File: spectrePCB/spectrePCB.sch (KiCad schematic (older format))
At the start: 21 parts

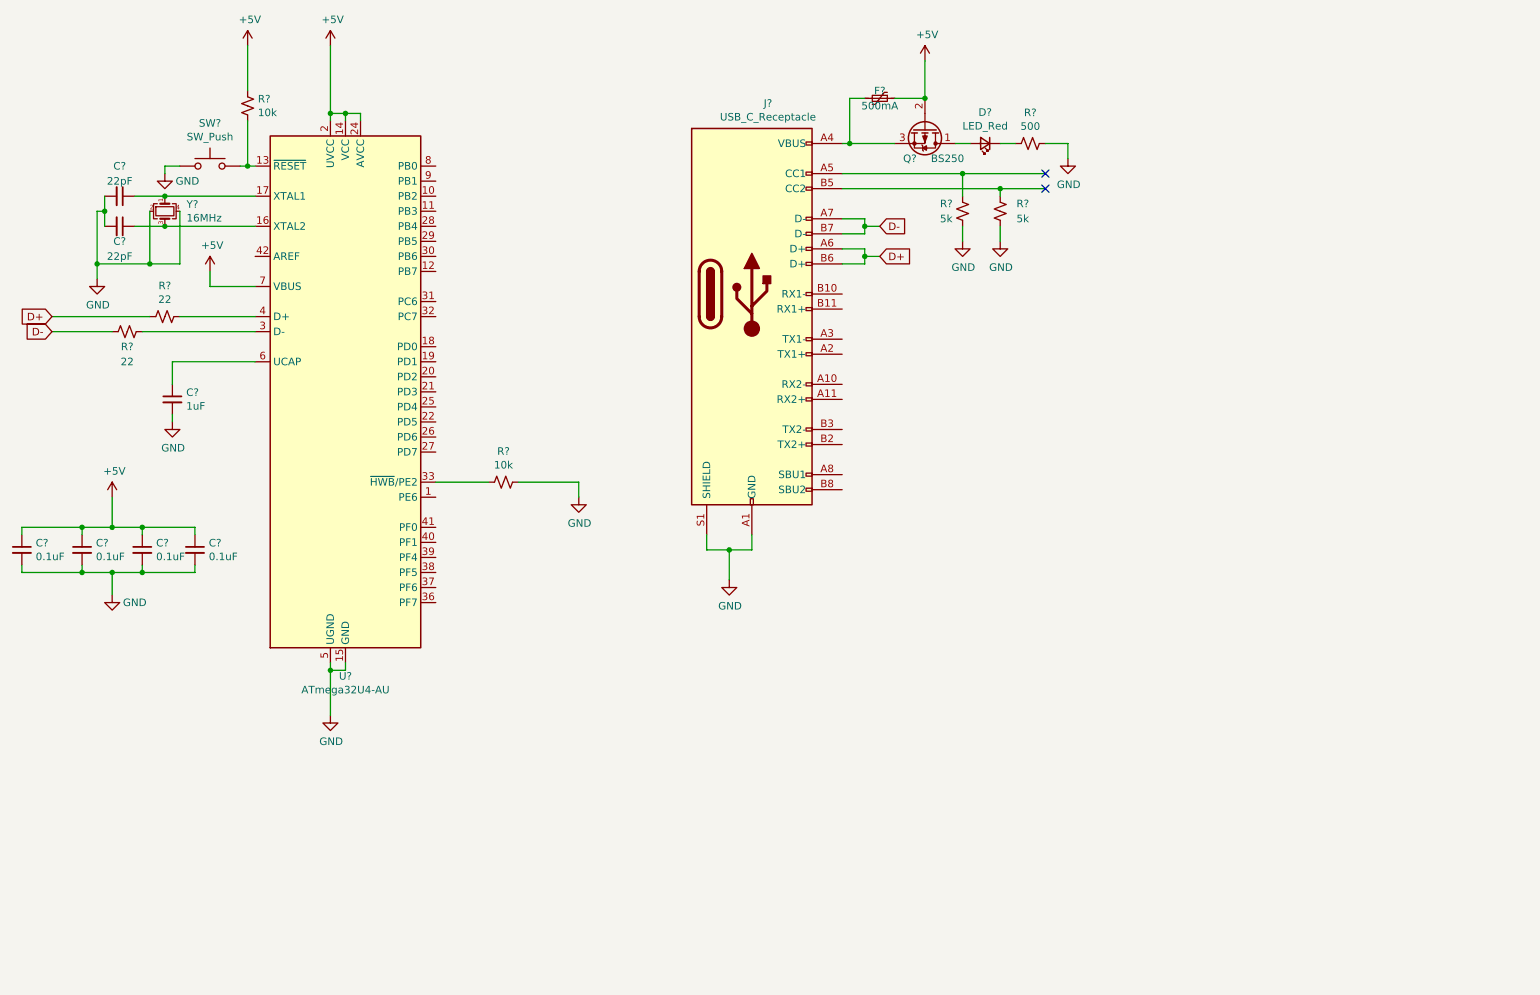
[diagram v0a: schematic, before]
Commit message: added switch and led matricies and pinouts to atmega
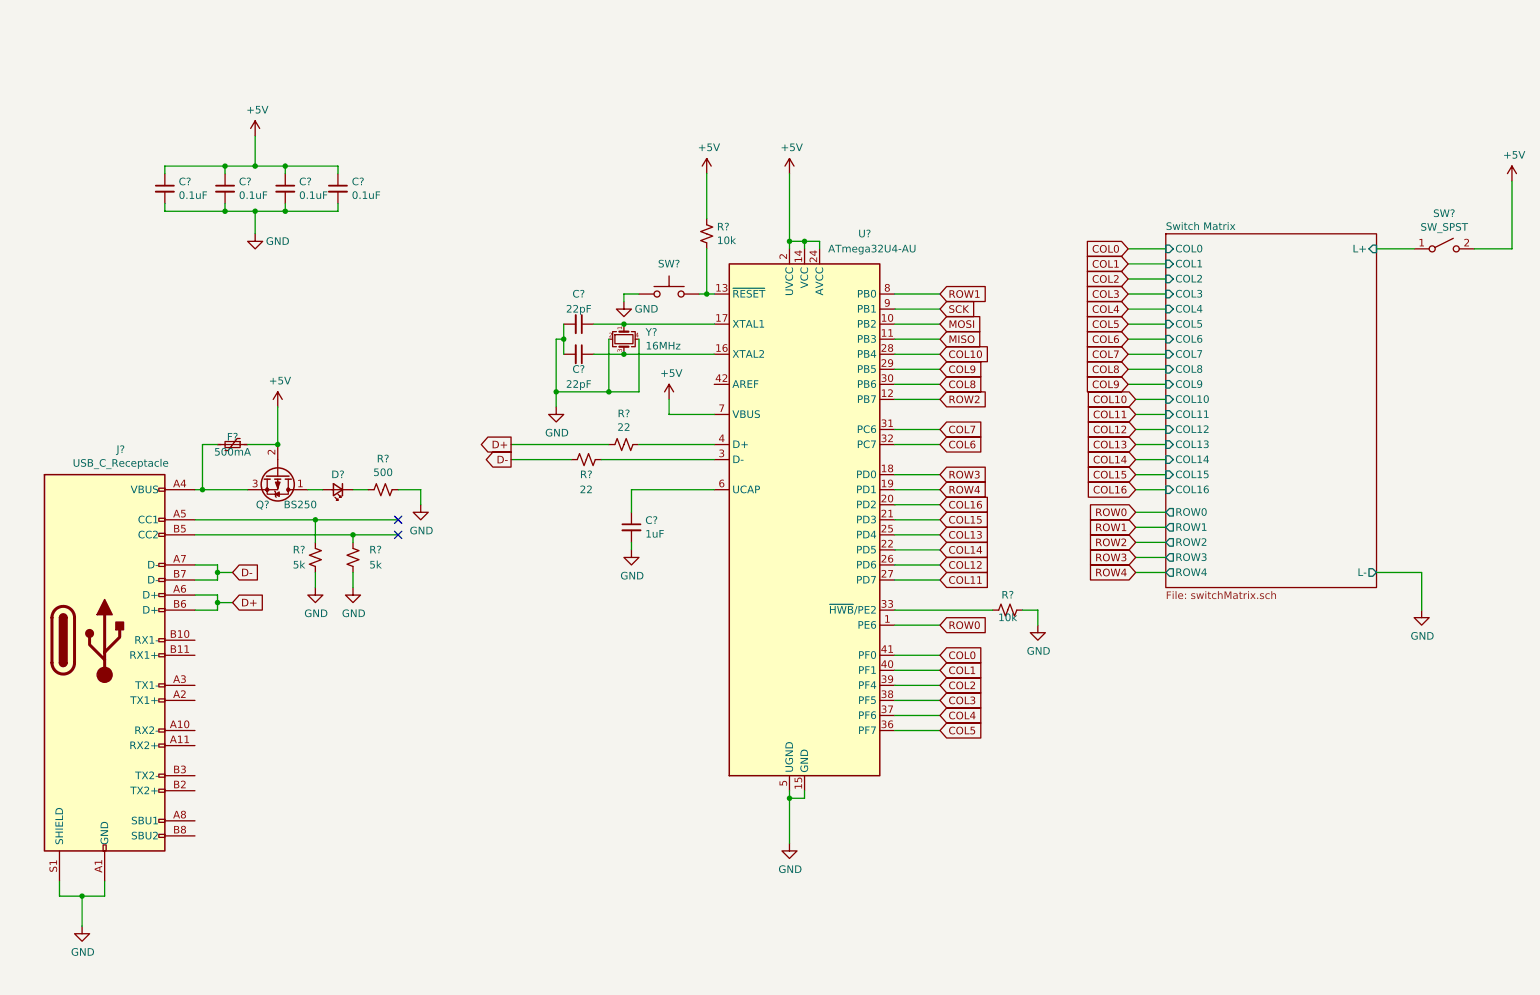
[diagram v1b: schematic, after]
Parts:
- added SW?: SW_SPST, symbol Switch:SW_SPST
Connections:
- net +5V: now also SW?.2 (B)
- net ROW0: now reaches U?.1 (PE6)
- net MOSI: now reaches U?.10 (PB2)
- net MISO: now reaches U?.11 (PB3)
- net ROW2: now reaches U?.12 (PB7)
- net ROW3: now reaches U?.18 (PD0)
- net ROW4: now reaches U?.19 (PD1)
- net COL16: now reaches U?.20 (PD2)
- net COL15: now reaches U?.21 (PD3)
- net COL14: now reaches U?.22 (PD5)
- net COL13: now reaches U?.25 (PD4)
- net COL12: now reaches U?.26 (PD6)
- net COL11: now reaches U?.27 (PD7)
- net COL10: now reaches U?.28 (PB4)
- net COL9: now reaches U?.29 (PB5)
- net COL8: now reaches U?.30 (PB6)
- net COL7: now reaches U?.31 (PC6)
- net COL6: now reaches U?.32 (PC7)
- net COL5: now reaches U?.36 (PF7)
- net COL4: now reaches U?.37 (PF6)
- net COL3: now reaches U?.38 (PF5)
- net COL2: now reaches U?.39 (PF4)
- net COL1: now reaches U?.40 (PF1)
- net COL0: now reaches U?.41 (PF0)
- net ROW1: now reaches U?.8 (PB0)
- net SCK: now reaches U?.9 (PB1)
- new net Switch Matrix/L+: SW?.1 (A)
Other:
- moved on the sheet: C?, D?, F?, J?, Q?, R?, SW?, U?, Y?

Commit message: finished capslock key and pin mapping. Rev1 done
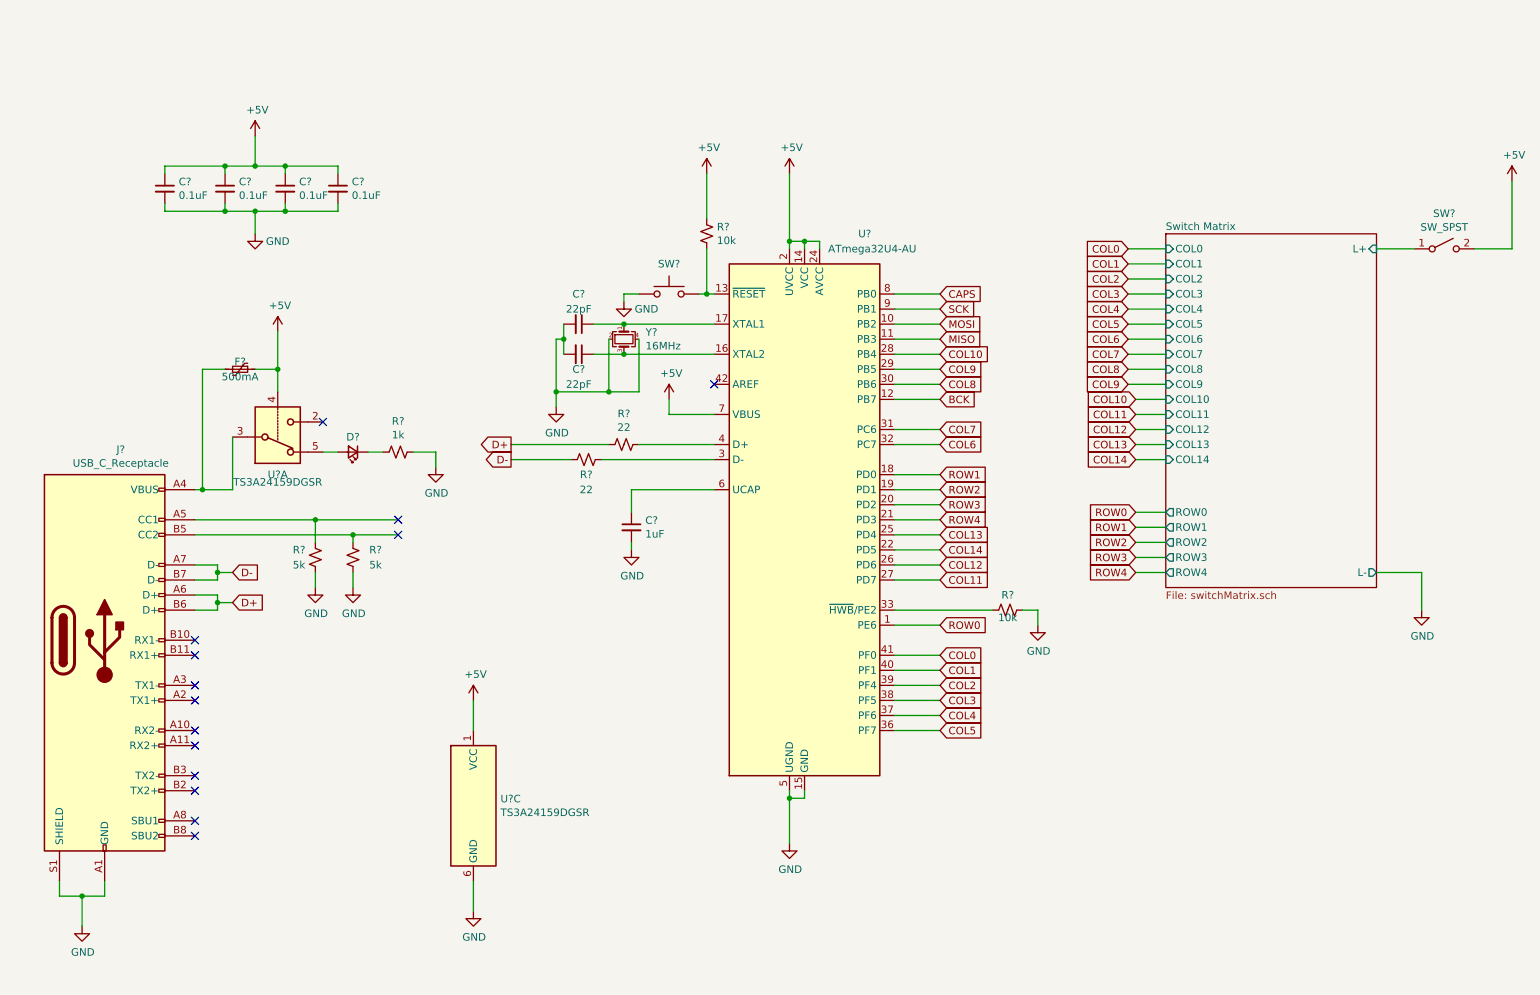
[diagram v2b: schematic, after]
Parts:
- removed Q?: BS250, Package_TO_SOT_THT:TO-92_Inline, symbol Transistor_FET:BS250
- added U? (x2): TS3A24159DGSR, Package_SO:TSSOP-10_3x3mm_P0.5mm, symbol Analog_Switch:TS3A24159DGSR
- R?: value 500 -> 1k
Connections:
- net COL15 is gone; now on net ROW4: U?.21 (PD3)
- net COL16 is gone; now on net ROW3: U?.20 (PD2)
- net +5V: now also U?.1 (VCC), U?.4
- net GND: now also U?.6 (GND)
- net ROW1: now also U?.18 (PD0); no longer U?.8 (PB0)
- net ROW2: now also U?.19 (PD1); no longer U?.12 (PB7)
- net ROW3: no longer U?.18 (PD0)
- net ROW4: no longer U?.19 (PD1)
- net at F?.2, J?.A4 (VBUS), J?.A9 (VBUS)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: now also U?.3
- net at D?.2 (A): now also U?.5
- new net BCK: U?.12 (PB7)
- new net CAPS: U?.8 (PB0)
- no-connect marks 2 -> 14
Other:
- moved on the sheet: D?, F?, R?
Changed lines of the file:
@@
 F20 "COL13" I L 8300 3500 50
 F21 "COL14" I L 8300 3600 50
-F22 "COL15" I L 8300 3700 50
-F23 "COL16" I L 8300 3800 50
-F24 "L+" I R 9700 2200 50
-F25 "L-" O R 9700 4350 50
+F22 "L+" I R 9700 2200 50
+F23 "L-" O R 9700 4350 50
 $EndSheet
-Connection ~ 2400 3500
-Wire Wire Line
-	2400 3500 2400 3250
-Wire Wire Line
-	3350 3800 3350 3900
-Wire Wire Line
-	3200 3800 3350 3800
-$Comp
-L power:GND #PWR?
-U 1 1 608320DA
-P 3350 3900
-F 0 "#PWR?" H 3350 3650 50  0001 C CNN
-F 1 "GND" H 3355 3727 50  0000 C CNN
-F 2 "" H 3350 3900 50  0001 C CNN
-F 3 "" H 3350 3900 50  0001 C CNN
-	1    3350 3900
-	1    0    0    -1
-$EndComp
-Wire Wire Line
-	2900 3800 3000 3800
-Wire Wire Line
-	2600 3800 2700 3800
-Wire Wire Line
-	2200 3500 2400 3500
-Wire Wire Line
-	1900 3800 2200 3800
+Wire Wire Line
+	1900 3800 2100 3800
 Connection ~ 1900 3800
 Wire Wire Line
-	1900 3500 2000 3500
-Wire Wire Line
-	1900 3800 1900 3500
-Wire Wire Line
 	1850 3800 1900 3800
-$Comp
-L Transistor_FET:BS250 Q?
-U 1 1 607DB3CA
-P 2400 3700
-F 0 "Q?" V 2600 3600 50  0000 C CNN
-F 1 "BS250" V 2600 3850 50  0000 C CNN
-F 2 "Package_TO_SOT_THT:TO-92_Inline" H 2600 3625 50  0001 L CIN
-F 3 "http://www.vishay.com/docs/70209/70209.pdf" H 2400 3700 50  0001 L CNN
-	1    2400 3700
-	0    1    1    0
-$EndComp
-$Comp
-L Device:R_Small_US R?
-U 1 1 607B83A1
-P 3100 3800
-F 0 "R?" V 2895 3800 50  0000 C CNN
-F 1 "500" V 2986 3800 50  0000 C CNN
-F 2 "" H 3100 3800 50  0001 C CNN
-F 3 "~" H 3100 3800 50  0001 C CNN
-	1    3100 3800
-	0    1    1    0
-$EndComp
 Connection ~ 2900 4100
 Wire Wire Line
@@
 $EndComp
 $Comp
-L power:+5V #PWR?
-U 1 1 606BD547
-P 2400 3250
-F 0 "#PWR?" H 2400 3100 50  0001 C CNN
-F 1 "+5V" H 2415 3423 50  0000 C CNN
-F 2 "" H 2400 3250 50  0001 C CNN
-F 3 "" H 2400 3250 50  0001 C CNN
-	1    2400 3250
-	1    0    0    -1
-$EndComp
-$Comp
-L Device:LED_Small D?
-U 1 1 606B968A
-P 2800 3800
-F 0 "D?" H 2800 3700 50  0000 C CNN
-F 1 "LED_Red" H 2800 3684 50  0001 C CNN
-F 2 "" V 2800 3800 50  0001 C CNN
-F 3 "~" V 2800 3800 50  0001 C CNN
-	1    2800 3800
-	-1   0    0    1
-$EndComp
-$Comp
 L Device:Polyfuse_Small F?
 U 1 1 606B6552
-P 2100 3500
-F 0 "F?" V 2050 3500 50  0000 C CNN
-F 1 "500mA" V 2150 3500 50  0000 C CNN
-F 2 "" H 2150 3300 50  0001 L CNN
-F 3 "~" H 2100 3500 50  0001 C CNN
-	1    2100 3500
+P 2150 3000
+F 0 "F?" V 2100 3000 50  0000 C CNN
+F 1 "500mA" V 2200 3000 50  0000 C CNN
+F 2 "" H 2200 2800 50  0001 L CNN
+F 3 "~" H 2150 3000 50  0001 C CNN
+	1    2150 3000
 	0    1    1    0
 $EndComp
@@
 Text GLabel 8100 3600 0    50   Input ~ 0
 COL14
-Text GLabel 8100 3700 0    50   Input ~ 0
-COL15
-Text GLabel 8100 3800 0    50   Input ~ 0
-COL16
 Text GLabel 8100 3950 0    50   Input ~ 0
 ROW0
@@
 Wire Wire Line
 	8100 3600 8300 3600
-Wire Wire Line
-	8100 3700 8300 3700
-Wire Wire Line
-	8100 3800 8300 3800
 Wire Wire Line
 	8100 3950 8300 3950
@@
 Text GLabel 6800 4200 2    50   Input ~ 0
 COL14
-Text GLabel 6800 4000 2    50   Input ~ 0
-COL15
-Text GLabel 6800 3900 2    50   Input ~ 0
-COL16
 Text GLabel 6800 4700 2    50   Input ~ 0
 ROW0
-Text GLabel 6800 2500 2    50   Input ~ 0
+Text GLabel 6800 3700 2    50   Input ~ 0
 ROW1
-Text GLabel 6800 3200 2    50   Input ~ 0
+Text GLabel 6800 3800 2    50   Input ~ 0
 ROW2
-Text GLabel 6800 3700 2    50   Input ~ 0
+Text GLabel 6800 3900 2    50   Input ~ 0
 ROW3
-Text GLabel 6800 3800 2    50   Input ~ 0
+Text GLabel 6800 4000 2    50   Input ~ 0
 ROW4
 Text GLabel 6800 2600 2    50   Input ~ 0
@@
 Wire Wire Line
 	6500 5400 6800 5400
+$Comp
+L Analog_Switch:TS3A24159DGSR U?
+U 3 1 605A1ABA
+P 3700 5900
+F 0 "U?" H 3880 5946 50  0000 L CNN
+F 1 "TS3A24159DGSR" H 3880 5855 50  0000 L CNN
+F 2 "Package_SO:TSSOP-10_3x3mm_P0.5mm" H 3700 5550 50  0001 C CNN
+F 3 "http://www.ti.com/lit/ds/symlink/ts3a24159.pdf" H 2650 5450 50  0001 C CNN
+	3    3700 5900
+	1    0    0    -1
+$EndComp
+Wire Wire Line
+	1900 3000 1900 3800
+Wire Wire Line
+	2400 3000 2250 3000
+Wire Wire Line
+	2100 3800 2100 3450
+Wire Wire Line
+	1900 3000 2050 3000
+Wire Wire Line
+	2400 3000 2400 3150
+$Comp
+L Analog_Switch:TS3A24159DGSR U?
+U 1 1 6059CE33
+P 2400 3550
+F 0 "U?" H 2400 3700 50  0000 C CNN
+F 1 "TS3A24159DGSR" H 2400 3750 50  0000 C CNN
+F 2 "Package_SO:TSSOP-10_3x3mm_P0.5mm" H 2400 3200 50  0001 C CNN
+F 3 "http://www.ti.com/lit/ds/symlink/ts3a24159.pdf" H 1350 3100 50  0001 C CNN
+	1    2400 3550
+	1    0    0    1
+$EndComp
+$Comp
+L Device:LED_Small D?
+U 1 1 606B968A
+P 2900 3550
+F 0 "D?" H 2900 3450 50  0000 C CNN
+F 1 "LED_Red" H 2900 3434 50  0001 C CNN
+F 2 "" V 2900 3550 50  0001 C CNN
+F 3 "~" V 2900 3550 50  0001 C CNN
+	1    2900 3550
+	-1   0    0    1
+$EndComp
+$Comp
+L Device:R_Small_US R?
+U 1 1 607B83A1
+P 3200 3550
+F 0 "R?" V 2995 3550 50  0000 C CNN
+F 1 "1k" V 3086 3550 50  0000 C CNN
+F 2 "" H 3200 3550 50  0001 C CNN
+F 3 "~" H 3200 3550 50  0001 C CNN
+	1    3200 3550
+	0    1    1    0
+$EndComp
+Wire Wire Line
+	2700 3550 2800 3550
+Wire Wire Line
+	3000 3550 3100 3550
+$Comp
+L power:GND #PWR?
+U 1 1 608320DA
+P 3450 3650
+F 0 "#PWR?" H 3450 3400 50  0001 C CNN
+F 1 "GND" H 3455 3477 50  0000 C CNN
+F 2 "" H 3450 3650 50  0001 C CNN
+F 3 "" H 3450 3650 50  0001 C CNN
+	1    3450 3650
+	1    0    0    -1
+$EndComp
+Wire Wire Line
+	3300 3550 3450 3550
+Wire Wire Line
+	3450 3550 3450 3650
+Connection ~ 2400 3000
+Wire Wire Line
+	2400 2750 2400 3000
+$Comp
+L power:+5V #PWR?
+U 1 1 606BD547
+P 2400 2750
+F 0 "#PWR?" H 2400 2600 50  0001 C CNN
+F 1 "+5V" H 2415 2923 50  0000 C CNN
+F 2 "" H 2400 2750 50  0001 C CNN
+F 3 "" H 2400 2750 50  0001 C CNN
+	1    2400 2750
+	1    0    0    -1
+$EndComp
+NoConn ~ 2700 3350
+NoConn ~ 1850 4800
+NoConn ~ 1850 4900
+NoConn ~ 1850 5100
+NoConn ~ 1850 5200
+NoConn ~ 1850 5400
+NoConn ~ 1850 5500
+NoConn ~ 1850 5700
+NoConn ~ 1850 5800
+NoConn ~ 1850 6000
+NoConn ~ 1850 6100
+NoConn ~ 5300 3100
+$Comp
+L power:+5V #PWR?
+U 1 1 606B51FC
+P 3700 5200
+F 0 "#PWR?" H 3700 5050 50  0001 C CNN
+F 1 "+5V" H 3715 5373 50  0000 C CNN
+F 2 "" H 3700 5200 50  0001 C CNN
+F 3 "" H 3700 5200 50  0001 C CNN
+	1    3700 5200
+	1    0    0    -1
+$EndComp
+$Comp
+L power:GND #PWR?
+U 1 1 606B6343
+P 3700 6600
+F 0 "#PWR?" H 3700 6350 50  0001 C CNN
+F 1 "GND" H 3705 6427 50  0000 C CNN
+F 2 "" H 3700 6600 50  0001 C CNN
+F 3 "" H 3700 6600 50  0001 C CNN
+	1    3700 6600
+	1    0    0    -1
+$EndComp
+Wire Wire Line
+	3700 5200 3700 5400
+Wire Wire Line
+	3700 6400 3700 6600
+Text GLabel 6800 3200 2    50   Input ~ 0
+BCK
+Text GLabel 6800 2500 2    50   Input ~ 0
+CAPS
 $EndSCHEMATC

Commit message: fixed big decoup cap not being big
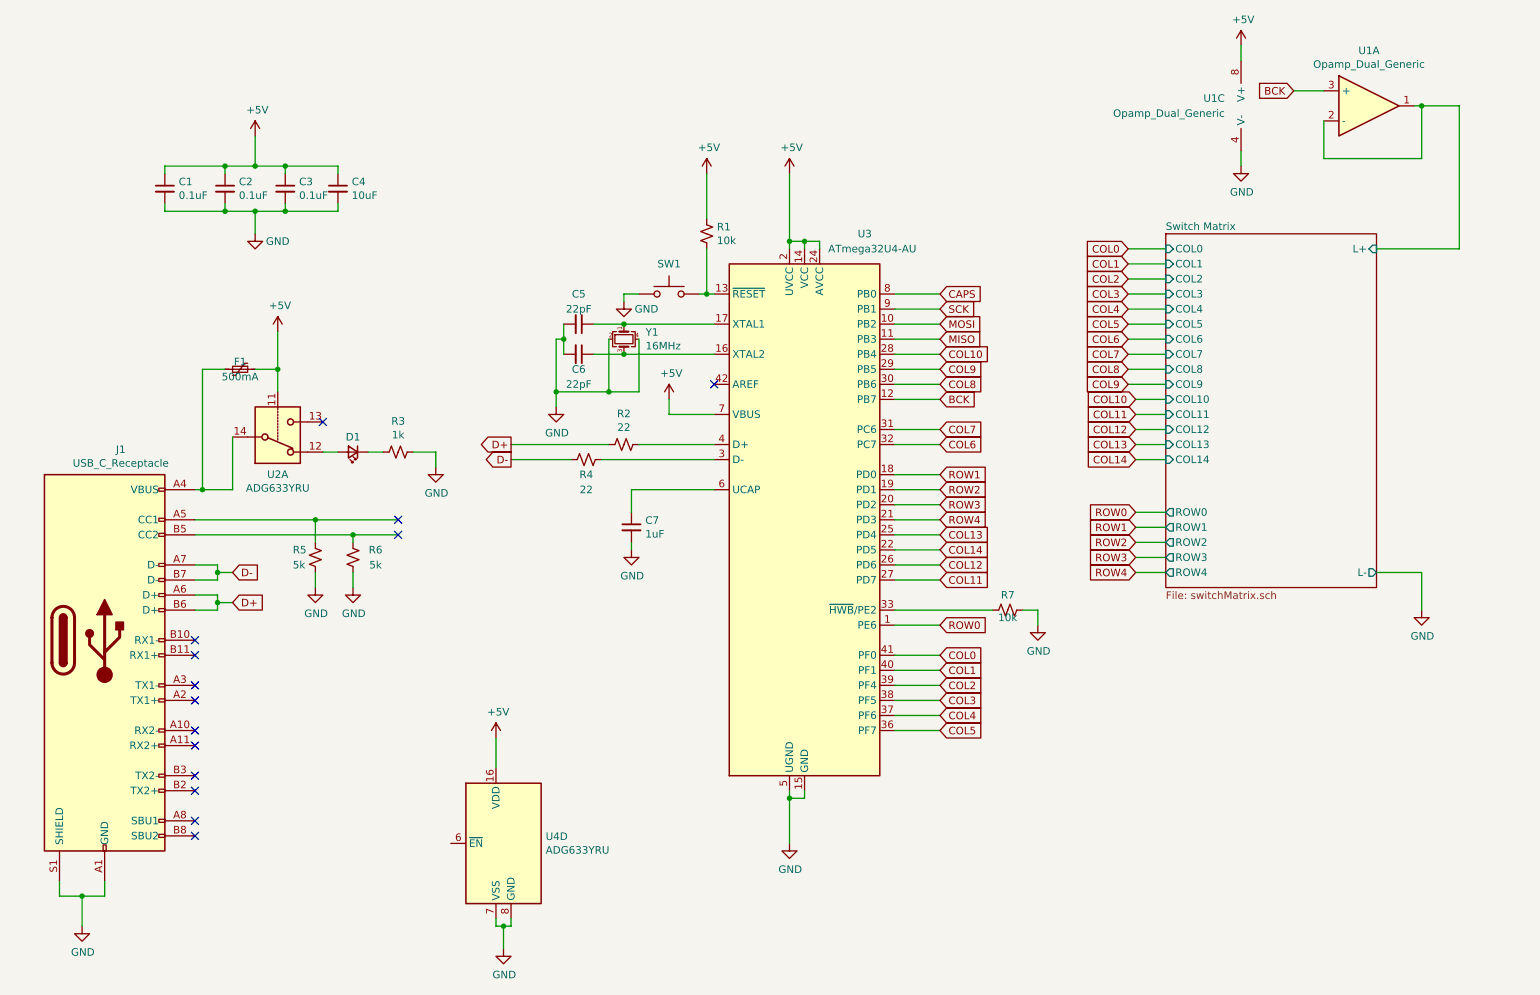
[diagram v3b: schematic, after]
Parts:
- removed SW?: SW_SPST, symbol Switch:SW_SPST
- removed U? (x2): TS3A24159DGSR, Package_SO:TSSOP-10_3x3mm_P0.5mm, symbol Analog_Switch:TS3A24159DGSR
- added U1: Opamp_Dual_Generic, symbol Device:Opamp_Dual_Generic
- added U2, U4: ADG633YRU, Package_SO:TSSOP-20_4.4x6.5mm_P0.65mm, symbol Analog_Switch:ADG633YRU
- C4: renamed from C?; value 0.1uF -> 10uF
- gave numbers to parts that had none: 19
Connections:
- net +5V: now also U1.8 (V+), U2.11, U4.16 (VDD)
- net BCK: now also U1.3 (+)
- net GND: now also U1.4 (V-), U4.7 (VSS), U4.8 (GND)
- net Switch Matrix/L+: now also U1.1, U1.2 (-)
- net at F1.2, J1.A4 (VBUS), J1.A9 (VBUS)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: now also U2.14
- net at D1.2 (A): now also U2.12
